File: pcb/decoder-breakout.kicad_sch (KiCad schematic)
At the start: 25 parts, among them J1 SM04B-SRSS-TB_LF__SN_, J2 SM04B-SRSS-TB_LF__SN_, J3 TBL009-254-08GY-2GY, Q1 BSS138, Q2 BSS138, U1 LS7866-S

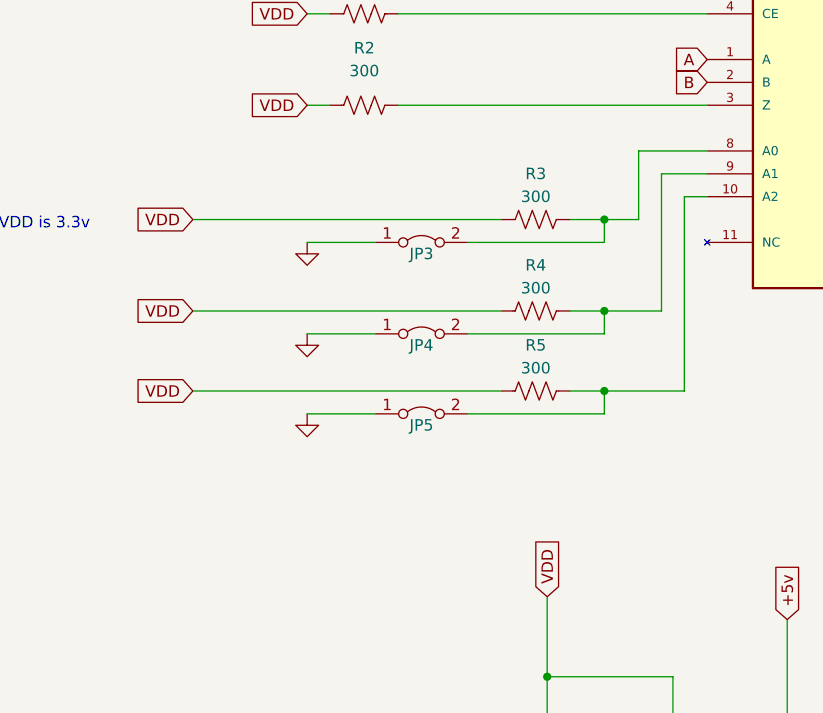
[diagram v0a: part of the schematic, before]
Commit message: WIP replace jumper pins with a single 2x3 group
- update schematic
- still needs PCB update
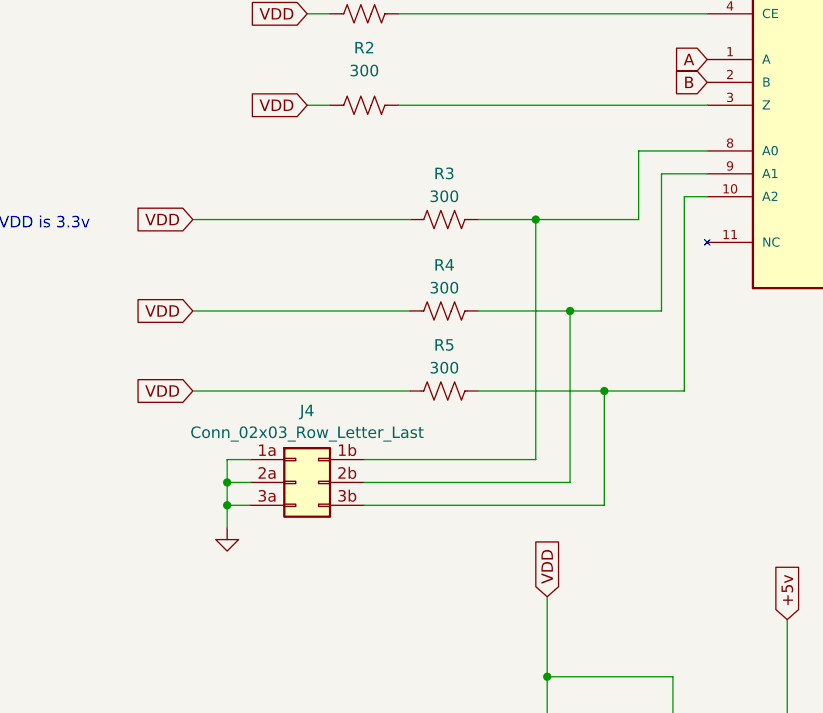
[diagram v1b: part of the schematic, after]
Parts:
- removed JP3, JP4, JP5: Jumper_2_Bridged, Connector_PinHeader_2.54mm:PinHeader_1x02_P2.54mm_Vertical, symbol Jumper:Jumper_2_Bridged
- added J4: Conn_02x03_Row_Letter_Last, Connector_PinHeader_2.54mm:PinHeader_2x03_P2.54mm_Vertical, symbol Connector_Generic:Conn_02x03_Row_Letter_Last
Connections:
- net GND: now also J4.1a (Pin_1a), J4.2a (Pin_2a), J4.3a (Pin_3a)
- net at R5.1, U1.10 (A2): now also J4.3b (Pin_3b)
- net at R3.1, U1.8 (A0): now also J4.1b (Pin_1b)
- net at R4.1, U1.9 (A1): now also J4.2b (Pin_2b)
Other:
- moved on the sheet: R3, R4, R5

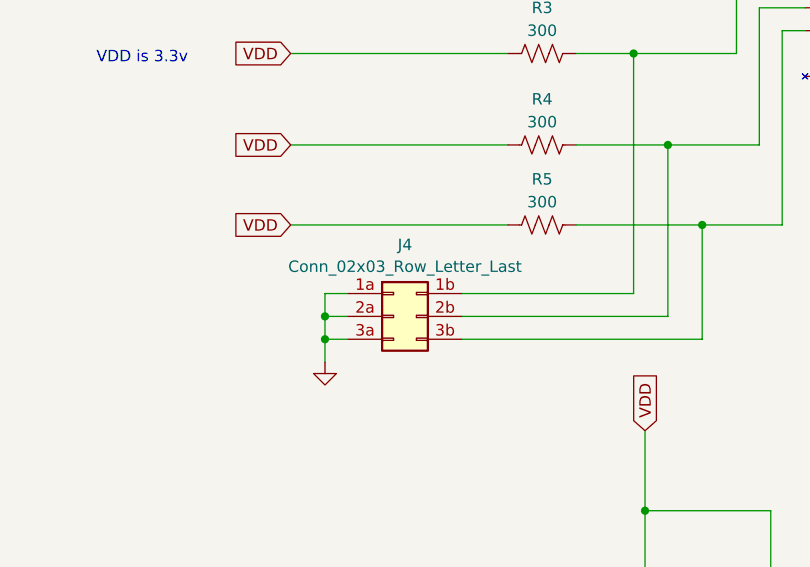
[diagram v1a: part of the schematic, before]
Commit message: WIP replacing pin headers on PCB with 2x3 group
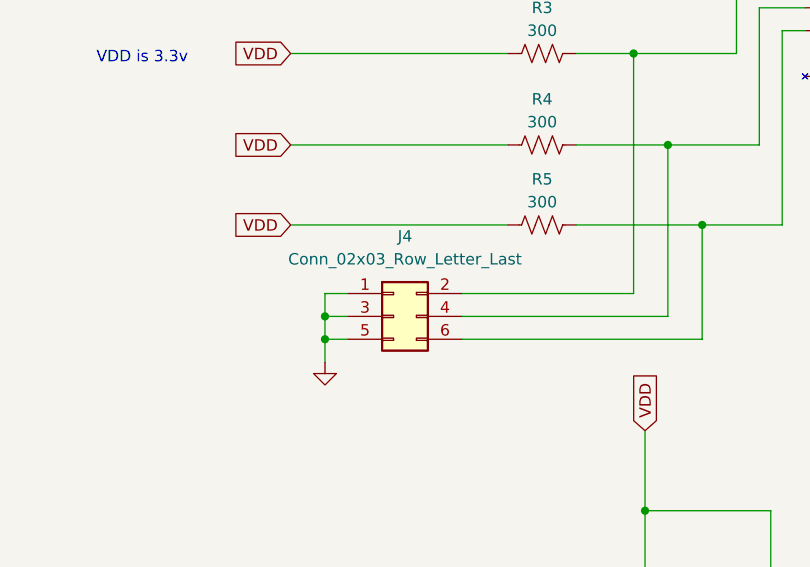
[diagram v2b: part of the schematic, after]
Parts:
- J4: symbol Connector_Generic:Conn_02x03_Row_Letter_Last -> Connector_Generic:Conn_02x03_Odd_Even
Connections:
- net GND: now also J4.1 (Pin_1), J4.3 (Pin_3), J4.5 (Pin_5); no longer J4.1a (Pin_1a), J4.2a (Pin_2a), J4.3a (Pin_3a)
- net at R5.1, U1.10 (A2): now also J4.6 (Pin_6); no longer J4.3b (Pin_3b)
- net at R3.1, U1.8 (A0): now also J4.2 (Pin_2); no longer J4.1b (Pin_1b)
- net at R4.1, U1.9 (A1): now also J4.4 (Pin_4); no longer J4.2b (Pin_2b)
